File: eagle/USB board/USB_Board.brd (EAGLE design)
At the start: 39 x 28.9 mm, 13 parts, among them U2 FT232RLSSOP

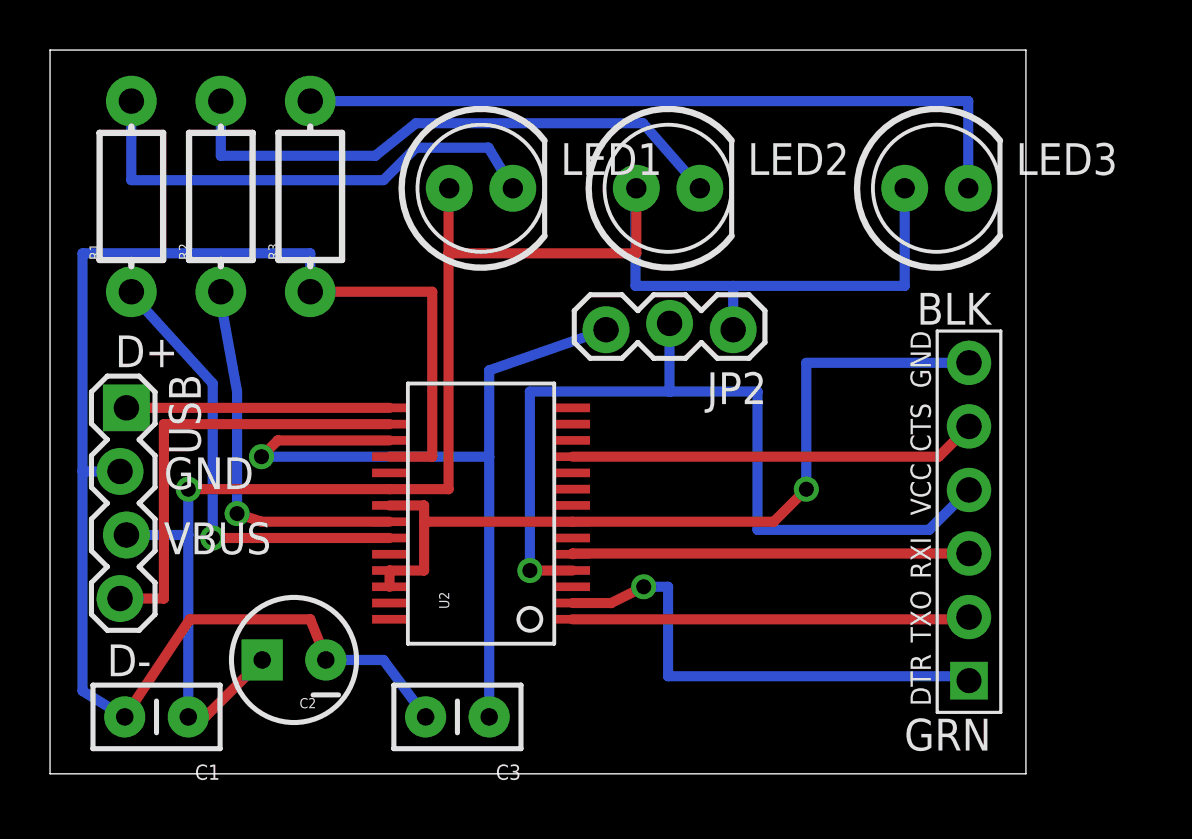
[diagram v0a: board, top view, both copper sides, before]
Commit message: First version of USB Board
Oops, forgot to put in drill holes.
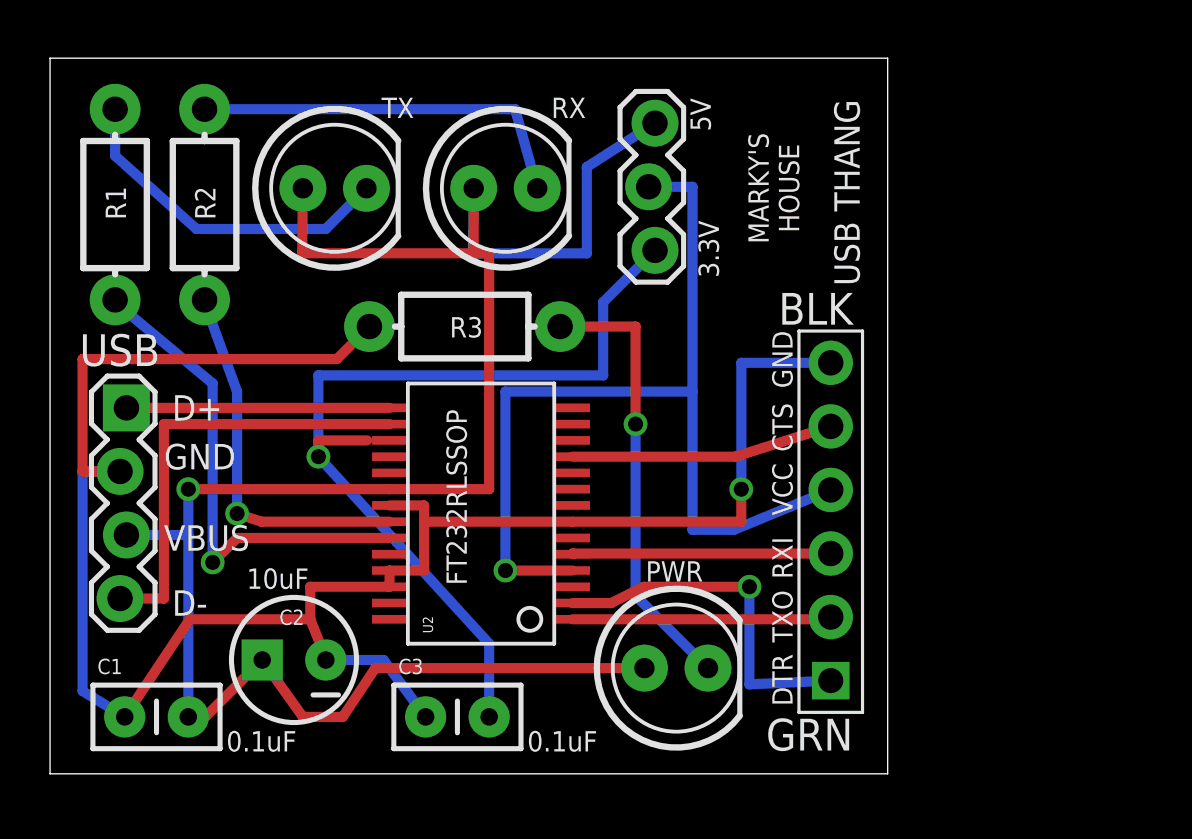
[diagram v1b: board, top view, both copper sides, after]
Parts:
- removed LED1, LED2, LED3: (no value), SparkFun-LED:LED5MM
- added PWR, RX, TX: (no value), SparkFun-LED:LED5MM
- moved JP2 8.75 mm to (24.1, 26.0), turned to 270 degrees
- moved R3 8.07 mm to (16.6, 17.9), turned to 0 degrees
- moved JP1 5.53 mm to (31.2, 10.1)
- moved R2 0.73 mm to (6.17, 22.8)
- moved R1 0.73 mm to (2.60, 22.8)
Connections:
- net 5V: now also PWR.A, RX.A, TX.A; no longer LED1.A, LED2.A, LED3.A
- net N$15: now also TX.K; no longer LED1.K
- net N$16: now also RX.K; no longer LED2.K
- net N$17: now also PWR.K; no longer LED3.K
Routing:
- net GND: track 94.6 -> 79.7 mm
- net 5V: track 68.4 -> 80.9 mm
- net N$17: track 29.8 -> 17.9 mm, vias 0 -> 1
- net N$16: track 23.0 -> 15.7 mm
- net N$15: track 19.9 -> 13.7 mm
- net N$9: track 16.3 -> 10.5 mm
- net N$8: track 15.9 -> 10.3 mm
- net N$10: track 19.7 -> 14.4 mm
- net N$7: track 15.9 -> 11.6 mm
- net N$11: track 35.3 -> 38.6 mm
- net 3.3V: track 33.3 -> 36.1 mm
- net N$13: track 18.2 -> 19.8 mm
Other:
- board size 39 x 28.9 mm -> 33.5 x 28.6 mm
- board text added: "0.1uF"
- board text added: "10uF"
- board text added: "3.3V"
- board text added: "5V"
- board text added: "FT232RLSSOP"
- board text added: "MARKY'S HOUSE"
- board text added: "USB THANG"
